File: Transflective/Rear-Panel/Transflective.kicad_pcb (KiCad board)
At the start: 2 copper layers, 155 x 88 mm, 13 parts, among them J1 feather long, J2 feather short, J3 feather long, J4 feather short, U1 Pico

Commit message: Reorganize Transflective directories
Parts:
- added J5: PermaProto, Transflective:PermaProto, F.Cu at (76.2, 104.0)
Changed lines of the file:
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@@
     (tracks 0)
     (zones 0)
-    (modules 13)
+    (modules 14)
     (nets 72)
   )
@@
     (add_net "Net-(U1-Pad9)")
   )
+  (module Transflective:PermaProto (layer F.Cu)
+    (at 76.2 104)
+    (fp_text reference J5 (at 0 2) (layer F.SilkS)
+      (effects (font (size 1 1) (thickness 0.15)))
+    )
+    (fp_text value PermaProto (at 0 -1.5) (layer F.Fab)
+      (effects (font (size 1 1) (thickness 0.15)))
+    )
+    (fp_line (start -40.5 -25.5) (end 40.5 -25.5) (layer F.CrtYd) (width 0.15))
+    (fp_line (start -40.5 25.5) (end 40.5 25.5) (layer F.CrtYd) (width 0.15))
+    (fp_line (start 40.5 -25.5) (end 40.5 25.5) (layer F.CrtYd) (width 0.15))
+    (fp_line (start -40.5 25.5) (end -40.5 -25.5) (layer F.CrtYd) (width 0.15))
+    (pad "" np_thru_hole circle (at -36.85 0) (size 3.2 3.2) (drill 3.2) (layers *.Cu *.Mask))
+    (pad "" np_thru_hole circle (at 36.85 0) (size 3.2 3.2) (drill 3.2) (layers *.Cu *.Mask))
+  )
   (module MCU_RaspberryPi_and_Boards:RPi_Pico_SMD_TH (layer F.Cu)

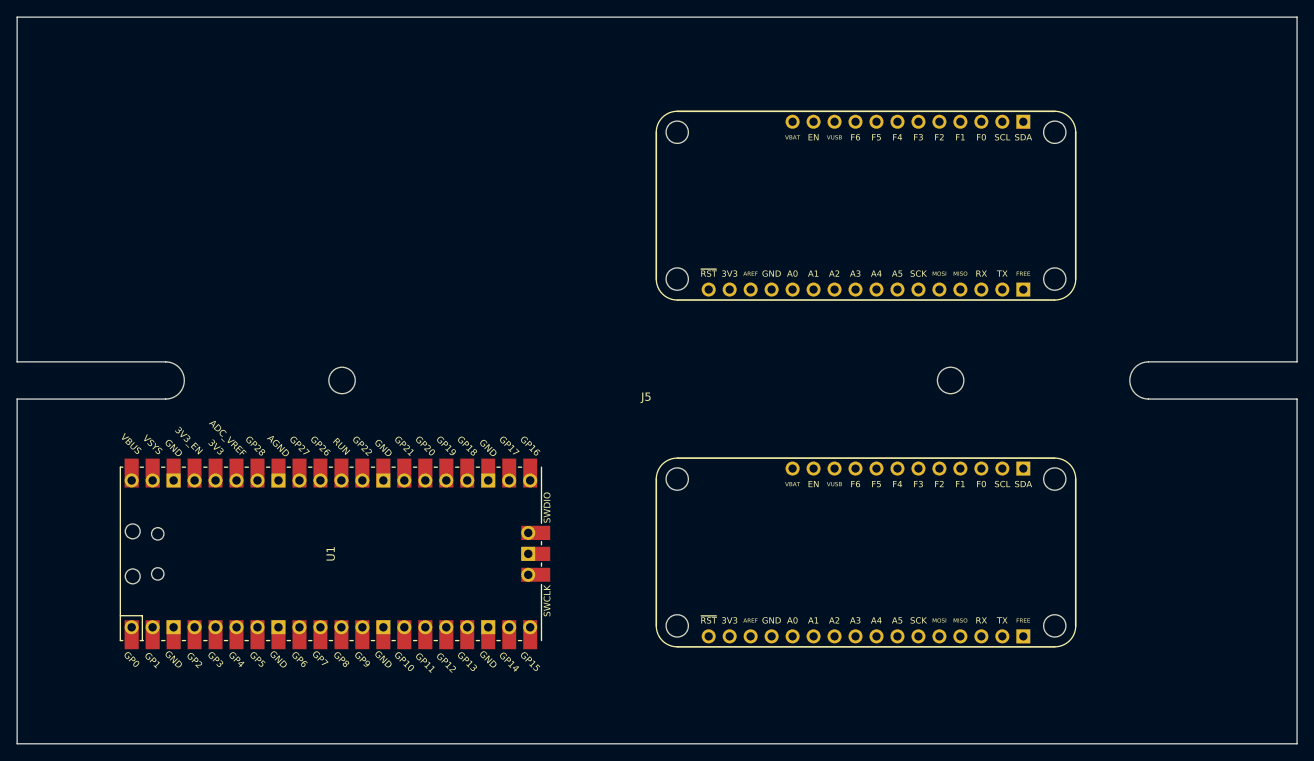
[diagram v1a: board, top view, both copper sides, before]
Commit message: Finish designing front and rear boards for Transflective LCD version
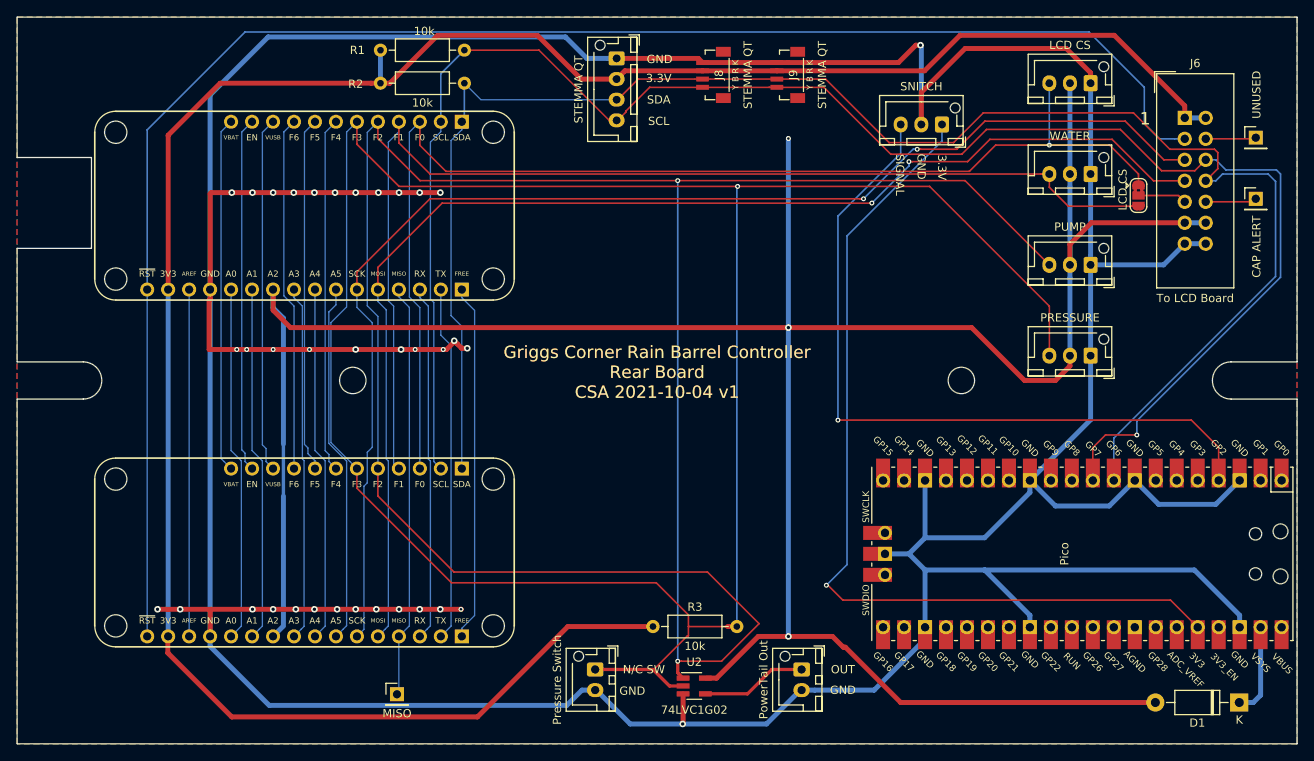
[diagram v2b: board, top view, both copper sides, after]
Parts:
- added D1: D_Schottky, Diode_THT:D_DO-41_SOD81_P10.16mm_Horizontal, F.Cu at (148.0, 143.0)
- added J10: STEMMA QT, Connector_JST:JST_XH_B04B-XH-AM_1x04_P2.50mm_Vertical, F.Cu at (72.6, 65.0)
- added J11: LCD CS, Connector_JST:JST_XH_B03B-XH-AM_1x03_P2.50mm_Vertical, F.Cu at (130.0, 68.0)
- added J12: WATER, Connector_JST:JST_XH_B03B-XH-AM_1x03_P2.50mm_Vertical, F.Cu at (130.0, 79.0)
- added J13: PUMP, Connector_JST:JST_XH_B03B-XH-AM_1x03_P2.50mm_Vertical, F.Cu at (130.0, 90.0)
- added J14: MISO, Connector_PinHeader_2.54mm:PinHeader_1x01_P2.54mm_Vertical, F.Cu at (46.0, 142.0)
- added J15: CAP ALERT, Connector_PinHeader_2.54mm:PinHeader_1x01_P2.54mm_Vertical, F.Cu at (150.0, 82.0)
- added J16: PRESSURE, Connector_JST:JST_XH_B03B-XH-AM_1x03_P2.50mm_Vertical, F.Cu at (130.0, 101.0)
- added J17: Pressure Switch, Connector_JST:JST_XH_B02B-XH-AM_1x02_P2.50mm_Vertical, F.Cu at (70.0, 139.0)
- added J18: PowerTail Out, Connector_JST:JST_XH_B02B-XH-AM_1x02_P2.50mm_Vertical, F.Cu at (95.0, 139.0)
- added J19: UNUSED, Connector_PinHeader_2.54mm:PinHeader_1x01_P2.54mm_Vertical, F.Cu at (150.0, 74.6)
- added J6: To LCD Board, Connector_IDC:IDC-Header_2x07_P2.54mm_Vertical, F.Cu at (141.4, 72.2)
- added J7: SNITCH, Connector_JST:JST_XH_B03B-XH-AM_1x03_P2.50mm_Vertical, F.Cu at (112.0, 73.0)
- added J8: STEMMA QT, Transflective:JST-SH-4-VERT-SMD, F.Cu at (83.0, 67.0)
- added J9: STEMMA QT, Transflective:JST-SH-4-VERT-SMD, F.Cu at (92.0, 67.0)
- added JP1: LCD CS, Jumper:SolderJumper-3_P1.3mm_Bridged2Bar12_RoundedPad1.0x1.5mm, F.Cu at (135.8, 81.6)
- added R1: 10k, Resistor_THT:R_Axial_DIN0207_L6.3mm_D2.5mm_P10.16mm_Horizontal, F.Cu at (44.0, 64.0)
- added R2: 10k, Resistor_THT:R_Axial_DIN0207_L6.3mm_D2.5mm_P10.16mm_Horizontal, F.Cu at (44.0, 68.0)
- added R3: 10k, Resistor_THT:R_Axial_DIN0207_L6.3mm_D2.5mm_P10.16mm_Horizontal, F.Cu at (77.0, 133.8)
- added U2: 74LVC1G02, Package_TO_SOT_SMD:SOT-23-5_HandSoldering, F.Cu at (82.0, 141.0)
- moved U1 91.0 mm to (129.0, 125.0), turned to 270 degrees
- moved J1 68.0 mm to (53.9, 93.0)
- moved J2 68.0 mm to (53.9, 72.7)
- moved J3 68.0 mm to (53.9, 135.0)
- moved J4 68.0 mm to (53.9, 114.7)
- moved REF** 68.0 mm to (11.9, 133.7)
- moved REF** 68.0 mm to (57.7, 115.9)
- moved REF** 68.0 mm to (57.7, 133.7)
- moved REF** 68.0 mm to (11.9, 115.9)
- moved REF** 68.0 mm to (57.7, 73.9)
- moved REF** 68.0 mm to (57.7, 91.7)
- moved REF** 68.0 mm to (11.9, 91.7)
- moved REF** 68.0 mm to (11.9, 73.9)
- moved J5 1.30 mm to (77.5, 104.0)
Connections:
- net /A2 renamed +5V
- U1 pad 10: Net-(U1-Pad10) -> /SCL
- U1 pad 13: Net-(U1-Pad13) -> GND
- U1 pad 18: Net-(U1-Pad18) -> GND
- U1 pad 23: Net-(U1-Pad23) -> GND
- U1 pad 28: Net-(U1-Pad28) -> GND
- U1 pad 3: Net-(U1-Pad3) -> GND
- U1 pad 36: Net-(U1-Pad36) -> /SNITCH_3V3
- U1 pad 38: Net-(U1-Pad38) -> GND
- U1 pad 4: Net-(U1-Pad4) -> /SNITCH_SIG
- U1 pad 42: Net-(U1-Pad42) -> GND
- U1 pad 8: Net-(U1-Pad8) -> GND
- U1 pad 9: Net-(U1-Pad9) -> /SDA
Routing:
- net GND: track 0.00 -> 603.8 mm, vias 0 -> 36
- net +5V: track 0.00 -> 320.8 mm, vias 0 -> 3
- net /F3: track 0.00 -> 273.3 mm, vias 0 -> 1
- net +3V3: track 0.00 -> 273.3 mm
- net /F2: track 0.00 -> 260.9 mm, vias 0 -> 2
- net /SCL: track 0.00 -> 213.7 mm, vias 0 -> 1
- net /SDA: track 0.00 -> 205.2 mm
- net /~RST: track 0.00 -> 200.3 mm
- net /SCK: track 0.00 -> 155.4 mm, vias 0 -> 2
- net /MOSI: track 0.00 -> 152.3 mm, vias 0 -> 2
- net /F0: track 0.00 -> 145.9 mm, vias 0 -> 1
- net /F1: track 0.00 -> 139.3 mm
- net /SNITCH_3V3: track 0.00 -> 108.7 mm, vias 0 -> 2
- net /SNITCH_SIG: track 0.00 -> 90.4 mm, vias 0 -> 1
- net /MISO: track 0.00 -> 50.2 mm
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- added copper zone on F.Cu, net +5V
- added copper zone on B.Cu, net GND
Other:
- outline, holes or cut-outs redrawn
- net class Default: clearance 0.2 -> 0.127; trace_width 0.25 -> 0.127; via_dia 0.8 -> 0.6; via_drill 0.4 -> 0.3
- net class Power added: clearance 0.2, trace_width 0.25, via_dia 0.8, via_drill 0.4
- rule pad_to_mask_clearance: 0.051 -> 0
- rule solder_mask_min_width: 0.25 -> 0.12
- rule trace_clearance: 0.2 -> 0.127
- rule trace_min: 0.2 -> 0.127
- rule via_min_size: 0.4 -> 0.6
- board text added: "1"
- board text added: "3.3V"
- board text added: "Griggs Corner Rain Barrel Controller Rear Board CSA 2021-10-04 v1"
- board text added: "N/C SW"
- board text added: "OUT"
- board text added: "SIGNAL"

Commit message: New Turbine, Level Amp boards (2 versions), and SMRT-Y Snitch board
Done with KiCAD 7; older designs migrated.
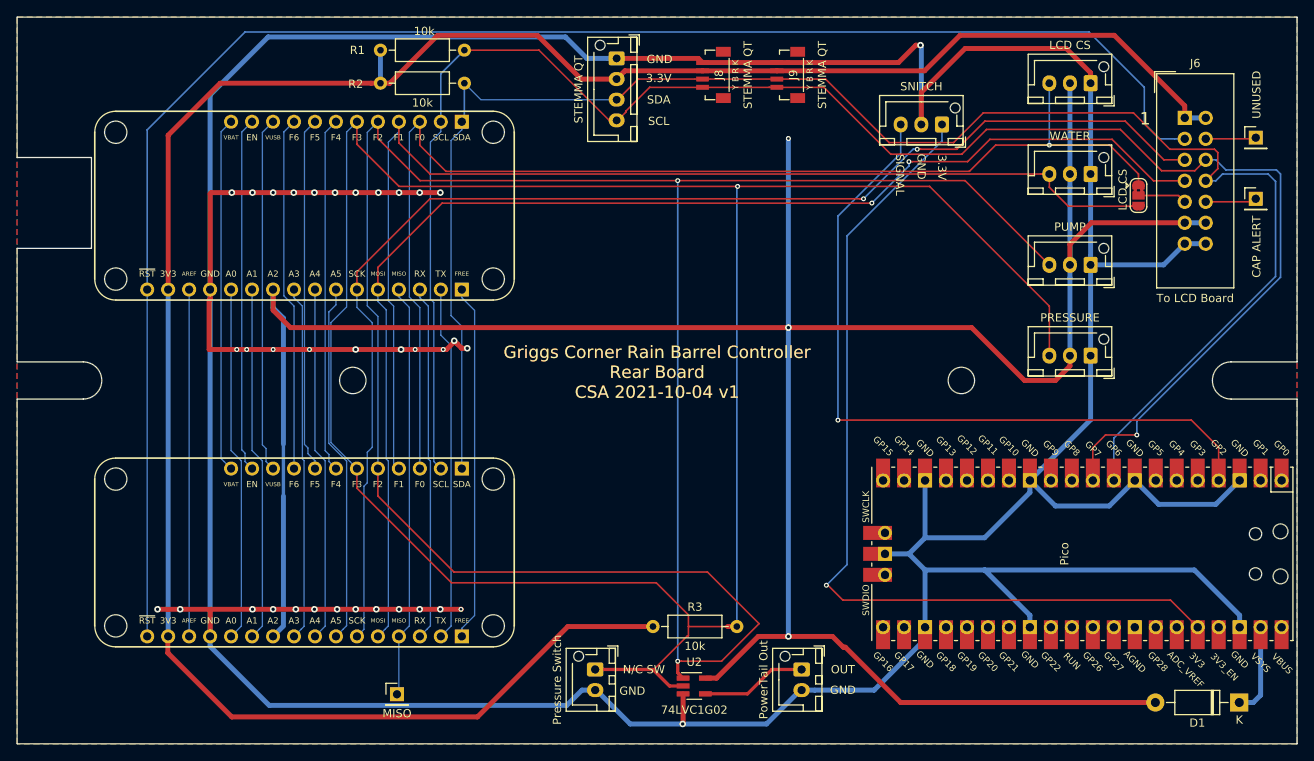
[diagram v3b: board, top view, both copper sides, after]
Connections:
- net /~RST renamed /~{RST}
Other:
- net class Default removed
- net class Power removed
- board text added: "~{RST}"
- board text removed: "~RST"
